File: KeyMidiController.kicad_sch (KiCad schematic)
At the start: 1 part

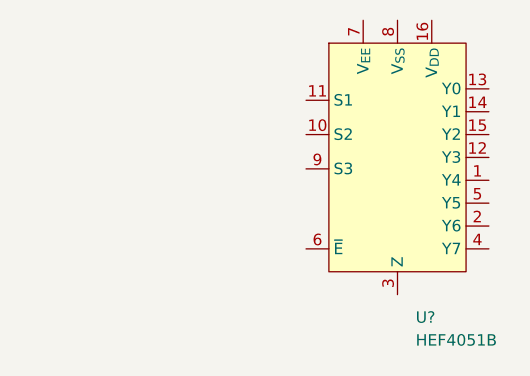
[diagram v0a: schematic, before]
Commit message: Added ReadMe
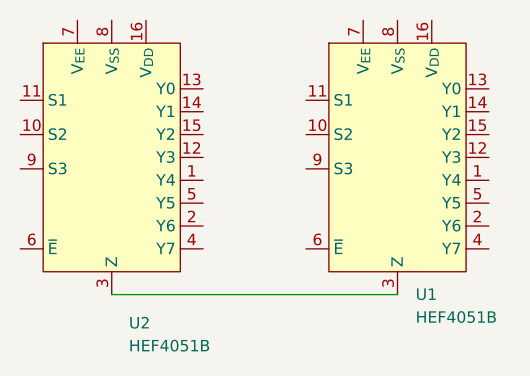
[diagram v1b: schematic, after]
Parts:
- added U2: HEF4051B, symbol Midi_Keyboard:HEF4051B
- gave numbers to parts that had none: 1
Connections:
- net at U1.3 (Z): now also U2.3 (Z)
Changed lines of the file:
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@@
     (rev "1.0")
+  )
+  (wire (pts (xy 108.585 119.38) (xy 140.335 119.38))
+    (stroke (width 0) (type default) (color 0 0 0 0))
   )
   (symbol (lib_id "Armaan_Library:HEF4051B") (at 140.335 107.95 0) (unit 1)
     (in_bom yes) (on_board yes) (fields_autoplaced)
-    (property "Reference" "U?" (id 0) (at 142.3544 121.92 0)
+    (property "Reference" "U1" (id 0) (at 142.3544 119.38 0)
       (effects (font (size 1.27 1.27)) (justify left))
     )
-    (property "Value" "HEF4051B" (id 1) (at 142.3544 124.46 0)
+    (property "Value" "HEF4051B" (id 1) (at 142.3544 121.92 0)
       (effects (font (size 1.27 1.27)) (justify left))
     )
@@
     (pin "9")
   )
+  (symbol (lib_id "Midi_Keyboard:HEF4051B") (at 108.585 107.95 0) (unit 1)
+    (in_bom yes) (on_board yes)
+    (property "Reference" "U2" (id 0) (at 110.49 122.555 0)
+      (effects (font (size 1.27 1.27)) (justify left))
+    )
+    (property "Value" "HEF4051B" (id 1) (at 110.49 125.095 0)
+      (effects (font (size 1.27 1.27)) (justify left))
+    )
+    (property "Footprint" "" (id 2) (at 108.585 82.55 0)
+      (effects (font (size 1.27 1.27)) hide)
+    )
+    (property "Datasheet" "" (id 3) (at 108.585 82.55 0)
+      (effects (font (size 1.27 1.27)) hide)
+    )
+    (pin "1")
+    (pin "10")
+    (pin "11")
+    (pin "12")
+    (pin "13")
+    (pin "14")
+    (pin "15")
+    (pin "16")
+    (pin "2")
+    (pin "3")
+    (pin "4")
+    (pin "5")
+    (pin "6")
+    (pin "7")
+    (pin "8")
+    (pin "9")
+  )
   (sheet_instances
     (path "/" (page "1"))
@@
   (symbol_instances
     (path "/a1150ae0-8bef-4db9-85b3-acc589657393"
-      (reference "U?") (unit 1) (value "HEF4051B") (footprint "")
+      (reference "U1") (unit 1) (value "HEF4051B") (footprint "")
+    )
+    (path "/e25a06cf-490b-4607-a3b3-a87e4dc7e259"
+      (reference "U2") (unit 1) (value "HEF4051B") (footprint "")
     )
   )

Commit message: Finally documenting the PCB
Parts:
- removed U2: HEF4051B, symbol Midi_Keyboard:HEF4051B
- added RV? (x8): R_Potentiometer, symbol Device:R_Potentiometer
- added RV? (x7): R_Potentiometer, Potentiometer_THT:Potentiometer_Bourns_PTA3043_Single_Slide, symbol Device:R_Potentiometer_MountingPin
- added RV?: R_Potentiometer, symbol Device:R_Potentiometer_MountingPin
- added U2, U?: HEF4051B, symbol Armaan_Library:HEF4051B
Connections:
- new net: RV?.2, RV?.2, RV?.2, RV?.2, RV?.2, RV?.2, RV?.2, RV?.2
- new net: RV?.1, U2.15 (Y2)
- new net: RV?.2, RV?.2, RV?.2, RV?.2, RV?.2, RV?.2, RV?.2, RV?.2, U2.16 (V_{DD})
- new net: RV?.1, U2.1 (Y4)
- new net: RV?.1, U2.13 (Y0)
- new net: RV?.1, U2.14 (Y1)
- new net: RV?.1, U2.5 (Y5)
- new net: RV?.1, U2.12 (Y3)
- new net: RV?.1, U2.2 (Y6)
- new net: RV?.1, U2.4 (Y7)

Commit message: Mass Update
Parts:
- removed RV? (x7): R_Potentiometer, Potentiometer_THT:Potentiometer_Bourns_PTA3043_Single_Slide, symbol Device:R_Potentiometer_MountingPin
- removed RV?: R_Potentiometer, symbol Device:R_Potentiometer_MountingPin
- added J?: DIN41612_02x08_AC_EvenPins, symbol Connector:DIN41612_02x08_AC_EvenPins
- added LINEAR, ROTARY, U?: HEF4051B, symbol Armaan_Library:HEF4051B
- added RV1, RV2, RV3, RV4, RV5, RV6, RV7, RV8: R_Potentiometer, symbol Device:R_Potentiometer
- added RV10, RV11, RV12, RV13, RV14, RV15, RV16, RV9, RV? (x8): R_Potentiometer, Potentiometer_THT:Potentiometer_Bourns_PTA3043_Single_Slide, symbol Device:R_Potentiometer_MountingPin
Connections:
- net at RV?.1: now also RV?.1, RV?.1, RV?.1, RV?.1, RV?.1, RV?.1, RV?.1, U1.7 (V_{EE}), U1.8 (V_{SS}), J?.Red (Pin_c6)
- net at RV?.3: now also RV?.3, RV?.3, RV?.3, RV?.3, RV?.3, RV?.3, RV?.3, U1.16 (V_{DD}), U2.16 (V_{DD}), U?.16 (V_{DD}), J?.Black, RV?.3, RV?.3, RV?.3, RV?.3, RV?.3, RV?.3, RV?.3, RV?.3
- net at U2.15 (Y2): now also RV?.2
- net at U2.1 (Y4): now also RV?.2
- net at U2.13 (Y0): now also RV?.2
- net at U?.10 (S2): now also U1.6 (~{E}), J?.Purple (Pin_c16)
- net at U?.11 (S1): now also U2.6 (~{E}), J?.Blue (Pin_c14)
- net at U?.3 (Z): now also U1.3 (Z), U2.3 (Z), J?.Brown (Pin_c4)
- net at U2.14 (Y1): now also RV?.2
- net at U2.5 (Y5): now also RV?.2
- net at U2.12 (Y3): now also RV?.2
- net at U2.10 (S2): now also U1.10 (S2), J?.Yellow (Pin_c10)
- net at U2.11 (S1): now also U1.11 (S1), J?.Orange (Pin_c8)
- net at U2.2 (Y6): now also RV?.2
- net at U2.4 (Y7): now also RV?.2
- net at U2.7 (V_{EE}): now also U2.8 (V_{SS})
- net at U2.9 (S3): now also U1.9 (S3), J?.Green (Pin_c12)
- net at U1.1 (Y4): now also RV?.2
- net at U1.12 (Y3): now also RV?.2
- net at U1.13 (Y0): now also RV?.2
- net at U1.14 (Y1): now also RV?.2
- net at U1.15 (Y2): now also RV?.2
- net at U1.2 (Y6): now also RV?.2
- net at U1.4 (Y7): now also RV?.2
- net at U1.5 (Y5): now also RV?.2
- new net: RV13.3, RV14.3, RV15.3, RV16.3
- new net: LINEAR.6 (~{E}), U?.11 (S1)
- new net: LINEAR.7 (V_{EE}), LINEAR.8 (V_{SS})
- new net: RV?.1, RV?.1, RV?.1, RV?.1, RV?.1, RV?.1, RV?.1, RV?.1
- new net: ROTARY.6 (~{E}), U?.10 (S2)
- new net: ROTARY.7 (V_{EE}), ROTARY.8 (V_{SS})
- new net: U?.7 (V_{EE}), U?.8 (V_{SS})
- new net Black: LINEAR.16 (V_{DD}), ROTARY.16 (V_{DD}), RV1.1, RV1.3, RV10.3, RV11.3, RV12.3, RV2.1, RV2.3, RV3.1, RV3.3, RV4.1, RV4.3, RV5.1, RV5.3, RV6.1, RV6.3, RV7.1, RV7.3, RV8.1, RV8.3, RV9.3, U?.16 (V_{DD})
- new net Green: LINEAR.9 (S3), ROTARY.9 (S3)
- new net Orange: LINEAR.11 (S1), ROTARY.11 (S1)
- new net Red: RV10.1, RV11.1, RV12.1, RV13.1, RV14.1, RV15.1, RV16.1, RV9.1
- new net Y0: RV12.2, RV4.2
- new net Y1: RV11.2, RV3.2
- new net Y2: RV10.2, RV2.2
- new net Y3: RV1.2, RV9.2
- new net Y4: RV16.2, RV8.2
- new net Y5: RV15.2, RV7.2
- new net Y6: RV14.2, RV6.2
- new net Y7: RV13.2, RV5.2
- new net Yellow: LINEAR.10 (S2), ROTARY.10 (S2)
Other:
- added sheet Mux (untitled.kicad_sch)
- moved on the sheet: RV?, U1, U2, U?
